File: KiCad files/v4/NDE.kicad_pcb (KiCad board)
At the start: 2 copper layers, 90 x 90 mm, 27 parts, among them J1 Nabíjací modul, J10 Conn_01x01_Socket, J11 Conn_01x01_Socket, J12 Conn_01x01_Socket, J13 Conn_01x01_Socket, J14 VM_Select, J2 Step-up input, J3 Step-up output, J6 Conn_01x05_Socket, J7 Conn_01x08_Socket, J8 Conn_01x20_Socket, J9 Conn_01x20_Socket, U1 LM7805_TO220

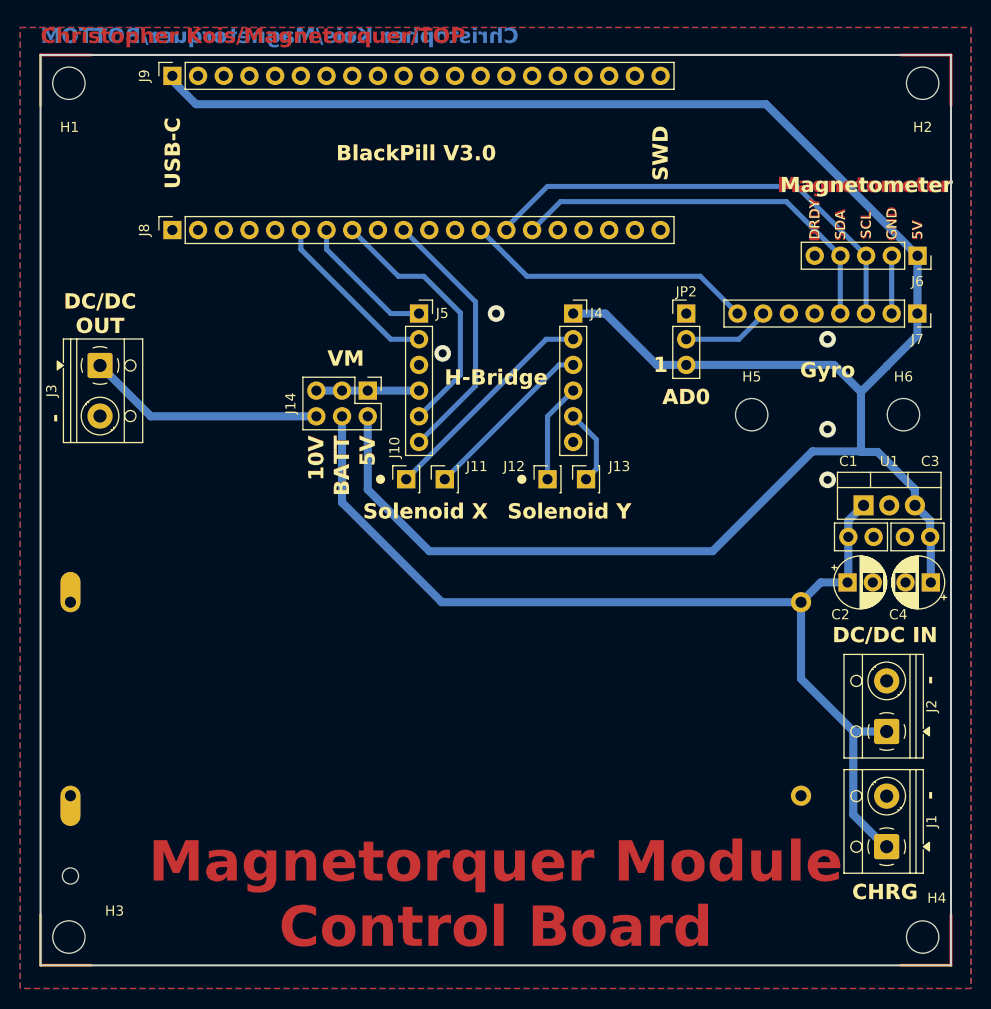
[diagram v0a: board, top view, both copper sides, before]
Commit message: Fixed unconnected GND of MCU and flipped H-bridge sockets
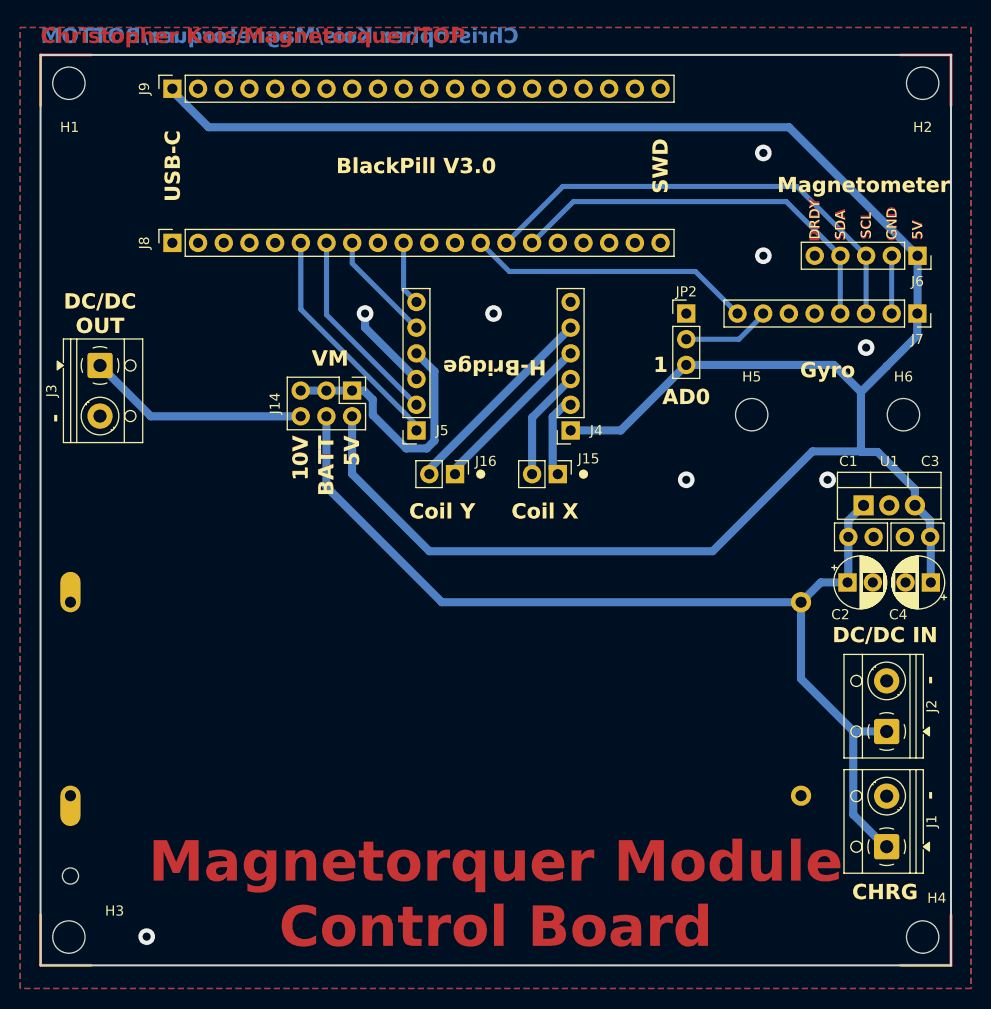
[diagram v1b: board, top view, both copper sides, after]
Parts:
- removed J10, J11, J12, J13: Conn_01x01_Socket, Connector_PinSocket_2.54mm:PinSocket_1x01_P2.54mm_Vertical
- added J15: Conn_01x02_Pin, Connector_PinHeader_2.54mm:PinHeader_1x02_P2.54mm_Vertical, F.Cu at (151.1, 91.4)
- added J16: Conn_01x02_Pin, Connector_PinHeader_2.54mm:PinHeader_1x02_P2.54mm_Vertical, F.Cu at (141.0, 91.4)
- moved J4 11.6 mm to (152.4, 87.1), turned to 180 degrees
- moved J5 11.6 mm to (137.2, 87.1), turned to 180 degrees
- moved J14 1.55 mm to (130.8, 83.2)
- moved J9 1.27 mm to (113.0, 53.3)
- moved J8 1.27 mm to (113.0, 68.6)
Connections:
- J5 pad 1: /BlackPill V3.0/A10 -> /BlackPill V3.0/A9
- J5 pad 2: /BlackPill V3.0/A9 -> /BlackPill V3.0/A10
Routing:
- net /BlackPill V3.0/A15: track 26.2 -> 6.37 mm
- net /H-mostík/VCC: track 10.2 -> 26.2 mm
- net /BlackPill V3.0/A11: track 26.0 -> 11.0 mm
- net /H-mostík/OUT1: track 22.2 -> 8.15 mm
- net /H-mostík/OUT4: track 7.59 -> 20.3 mm
- net GND: track 5.72 -> 14.3 mm, vias 5 -> 8
- net /H-mostík/OUT3: track 9.82 -> 16.7 mm
- net /H-mostík/OUT2: track 17.4 -> 11.0 mm
- net /BlackPill V3.0/A9: track 17.3 -> 23.3 mm
- net /BlackPill V3.0/A10: track 13.7 -> 19.7 mm
- net +10V: track 23.5 -> 21.9 mm
- net +BATT: track 102.7 -> 103.3 mm
- net +5V: track 214.0 -> 214.6 mm
- net /GY_INT: track 28.8 -> 28.3 mm
- net /SDA1: track 39.6 -> 40.1 mm
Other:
- board text added: "Coil X"
- board text added: "Coil Y"
- board text removed: "Solenoid X"
- board text removed: "Solenoid Y"
